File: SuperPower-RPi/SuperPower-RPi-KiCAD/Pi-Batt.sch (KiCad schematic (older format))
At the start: 9 parts, among them J2 Conn_01x02, J4 Conn_01x02, Q1 SSM3J328R, Q6 Q_NMOS_GSD

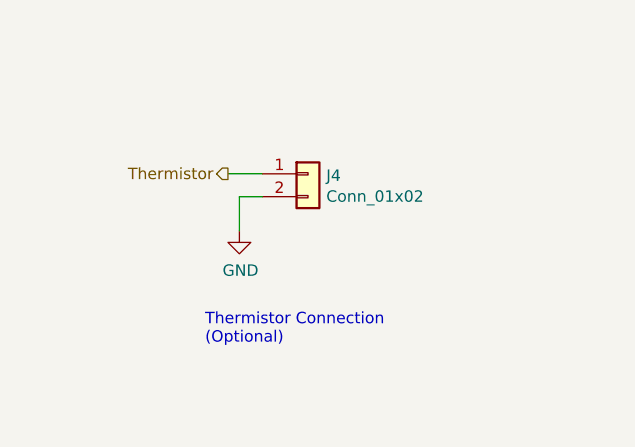
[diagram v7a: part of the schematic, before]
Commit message: Added Thermistor voltage divider and jumper on CE.
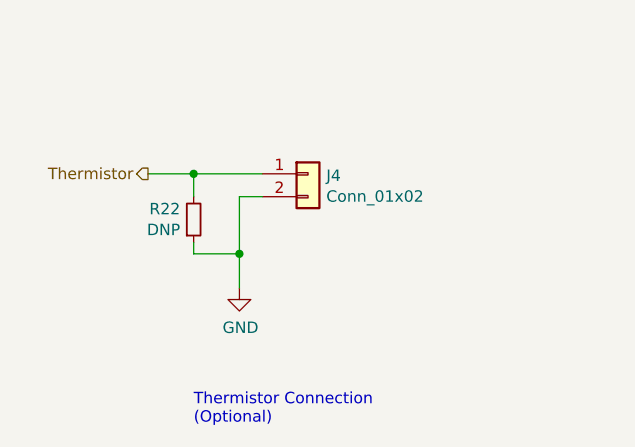
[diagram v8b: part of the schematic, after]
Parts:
- added R22: DNP, Resistor_SMD:R_0603_1608Metric, symbol Device:R_Small
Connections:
- net GND: now also R22.1
- net Thermistor: now also R22.2
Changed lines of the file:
@@
 $Descr A4 11693 8268
 encoding utf-8
-Sheet 7 8
+Sheet 6 8
 Title ""
 Date ""
@@
 	7700 2500 7950 2500
 Connection ~ 7700 2750
-Text HLabel 4050 5900 0    50   Output ~ 0
+Text HLabel 3700 5900 0    50   Output ~ 0
 Thermistor
 $Comp
@@
 $EndComp
 Wire Wire Line
-	4200 5900 4050 5900
+	4200 5900 3900 5900
 $Comp
 L power:GND #PWR015
 U 1 1 5F7AD85C
-P 4100 6150
-F 0 "#PWR015" H 4100 5900 50  0001 C CNN
-F 1 "GND" H 4105 5977 50  0000 C CNN
-F 2 "" H 4100 6150 50  0001 C CNN
-F 3 "" H 4100 6150 50  0001 C CNN
-	1    4100 6150
-	1    0    0    -1
-$EndComp
-Wire Wire Line
-	4100 6150 4100 6000
+P 4100 6400
+F 0 "#PWR015" H 4100 6150 50  0001 C CNN
+F 1 "GND" H 4105 6227 50  0000 C CNN
+F 2 "" H 4100 6400 50  0001 C CNN
+F 3 "" H 4100 6400 50  0001 C CNN
+	1    4100 6400
+	1    0    0    -1
+$EndComp
+Wire Wire Line
+	4100 6400 4100 6250
 Wire Wire Line
 	4100 6000 4200 6000
@@
 Text Notes 5150 4100 0    50   ~ 0
 Reverse Polarity Protection
-Text Notes 3950 6650 0    50   ~ 0
+Text Notes 3900 7000 0    50   ~ 0
 Thermistor Connection\n(Optional)
 Text Notes 7650 3650 0    50   ~ 0
 Battery Connection
+$Comp
+L Device:R_Small R?
+U 1 1 5FBB505A
+P 3900 6100
+AR Path="/5F6AC481/5FBB505A" Ref="R?"  Part="1"
+AR Path="/5F6AC644/5FBB505A" Ref="R22"  Part="1"
+F 0 "R22" H 3841 6054 50  0000 R CNN
+F 1 "DNP" H 3841 6145 50  0000 R CNN
+F 2 "Resistor_SMD:R_0603_1608Metric" H 3900 6100 50  0001 C CNN
+F 3 "~" H 3900 6100 50  0001 C CNN
+	1    3900 6100
+	1    0    0    1
+$EndComp
+Wire Wire Line
+	3900 6000 3900 5900
+Connection ~ 3900 5900
+Wire Wire Line
+	3900 5900 3700 5900
+Wire Wire Line
+	3900 6250 3900 6200
+Wire Wire Line
+	3900 6250 4100 6250
+Connection ~ 4100 6250
+Wire Wire Line
+	4100 6250 4100 6000
 $EndSCHEMATC
